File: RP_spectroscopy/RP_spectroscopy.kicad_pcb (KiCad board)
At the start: 2 copper layers, 90.5 x 116.6 mm, 79 parts, among them J1 Extension connector 1, J10 Conn_Coaxial, J2 Extension connector 2, J3 Conn_Coaxial, J4 Conn_Coaxial, J5 Conn_Coaxial, J6 Conn_Coaxial, J7 Molex PicoBlade, J8 Molex PicoBlade, J9 Conn_Coaxial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

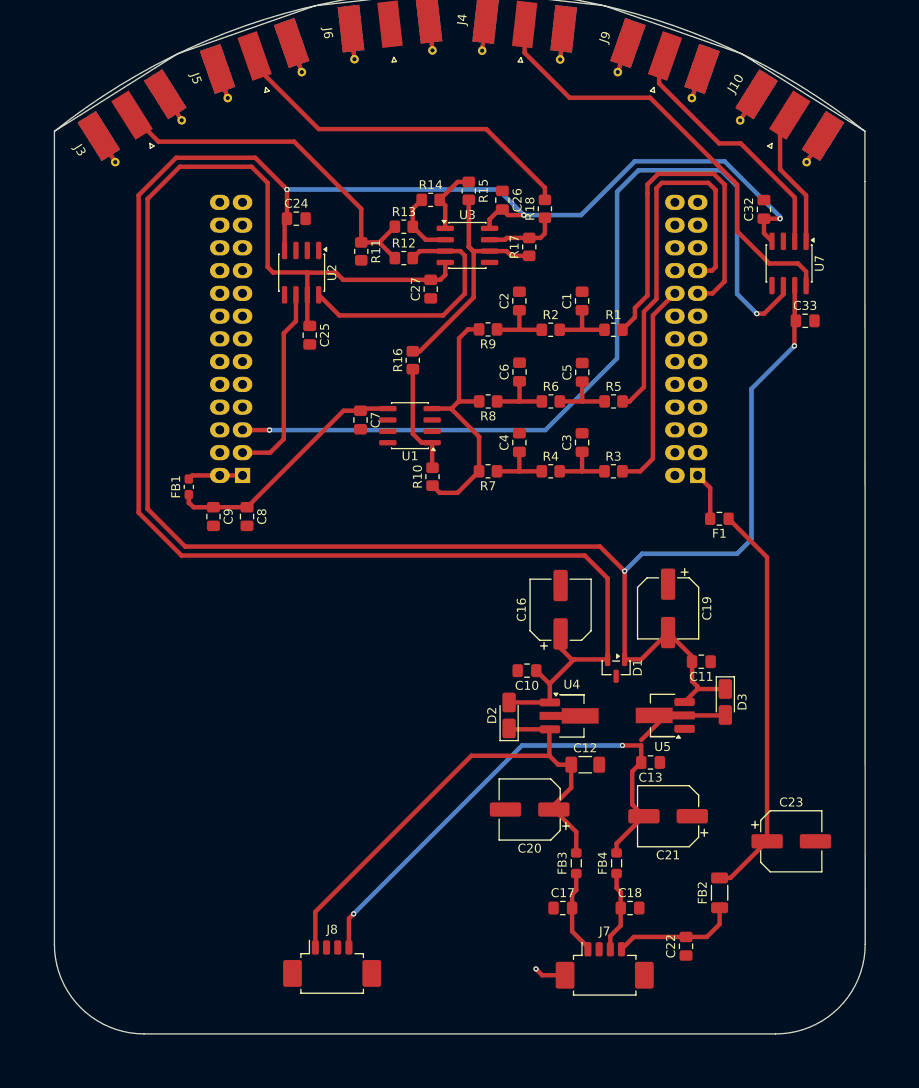
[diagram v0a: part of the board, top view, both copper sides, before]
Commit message: Modified the layout in order to give space in the upper part for the filter + amplification
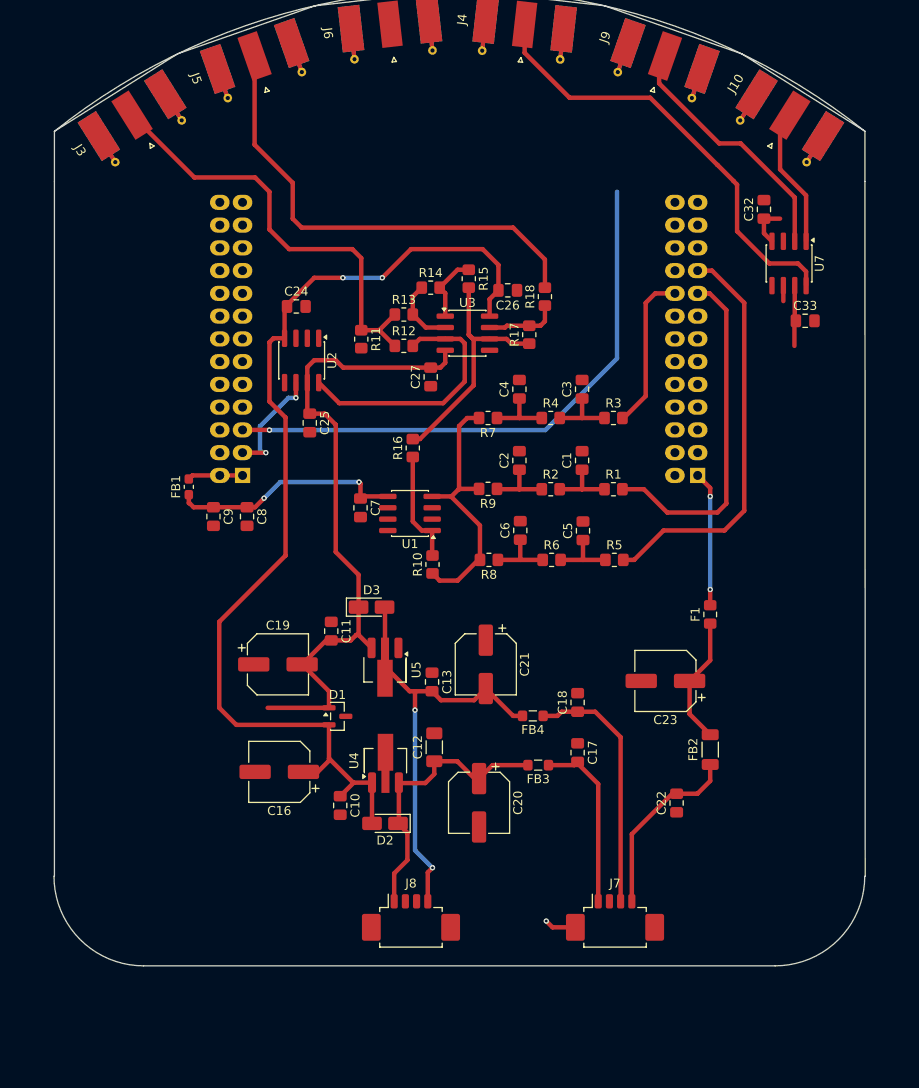
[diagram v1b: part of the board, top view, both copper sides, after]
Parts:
- moved C19 44.0 mm to (115.0, 108.8), turned to 0 degrees
- moved C11 41.5 mm to (120.9, 105.0), turned to -90 degrees
- moved D3 40.9 mm to (125.4, 102.4), turned to 0 degrees
- moved C16 36.2 mm to (115.1, 120.8), turned to 180 degrees
- moved D1 31.6 mm to (121.6, 114.5), turned to 0 degrees
- moved U5 31.4 mm to (126.9, 109.4), turned to -90 degrees
- moved C21 26.5 mm to (138.2, 108.8), turned to -90 degrees
- moved C13 26.0 mm to (132.2, 110.7), turned to -90 degrees
- moved C10 25.7 mm to (121.9, 124.5), turned to -90 degrees
- moved C18 23.7 mm to (148.4, 113.0), turned to 90 degrees
- moved C23 22.8 mm to (158.2, 110.6), turned to 180 degrees
- moved U4 21.4 mm to (127.0, 119.5), turned to 90 degrees
- moved FB4 18.9 mm to (143.4, 114.5), turned to 180 degrees
- moved D2 18.4 mm to (126.9, 126.5), turned to 180 degrees
- moved C1 17.8 mm to (148.9, 86.0)
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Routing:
- net -5VA: track 218.6 -> 80.6 mm, vias 2 -> 0
- net +5VA: track 218.2 -> 121.1 mm, vias 3 -> 2
- net Multiplex switch: track 98.8 -> 64.5 mm, vias 2 -> 1
- net +5V: track 44.8 -> 14.3 mm
- net +15V: track 59.4 -> 32.0 mm
- net Net-(J7-Pin_3): track 9.12 -> 28.3 mm
- net -15V: track 68.6 -> 49.8 mm
- net Summed signals: track 40.4 -> 54.1 mm
- net Net-(J7-Pin_1): track 9.37 -> 19.9 mm
- net Net-(J2-Pin_1): track 5.42 -> 15.1 mm, vias 0 -> 2
- net Sweep/Fast PID: track 40.6 -> 49.7 mm
- net Ramp sign: track 21.9 -> 13.1 mm, vias 0 -> 2
- net Net-(J7-Pin_4): track 13.9 -> 20.5 mm
- net Big offset: track 23.5 -> 17.7 mm
- net Slow integrator: track 41.3 -> 38.7 mm
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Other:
- board size 90.5 x 116.6 mm -> 90.6 x 109 mm

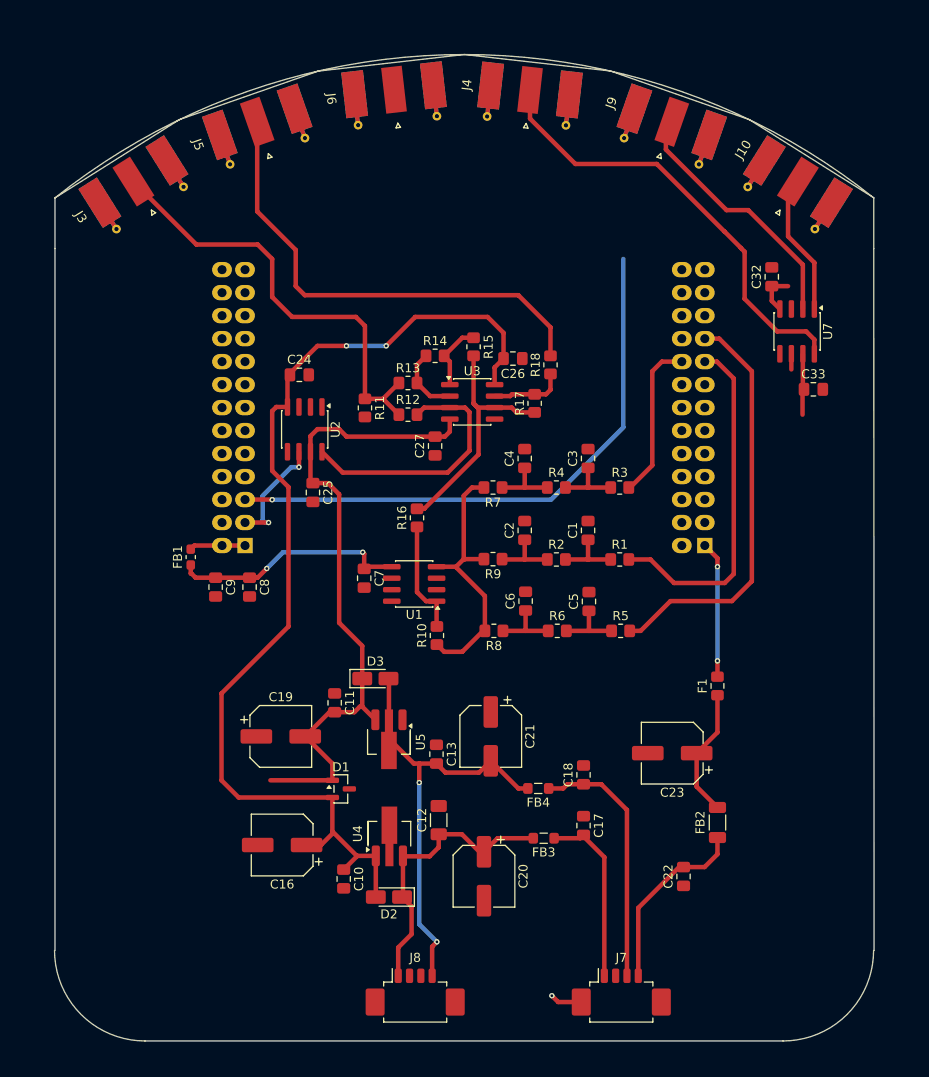
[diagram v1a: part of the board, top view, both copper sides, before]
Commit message: Compacted power and sumator branches. Started to check the RP measurement and compatibility
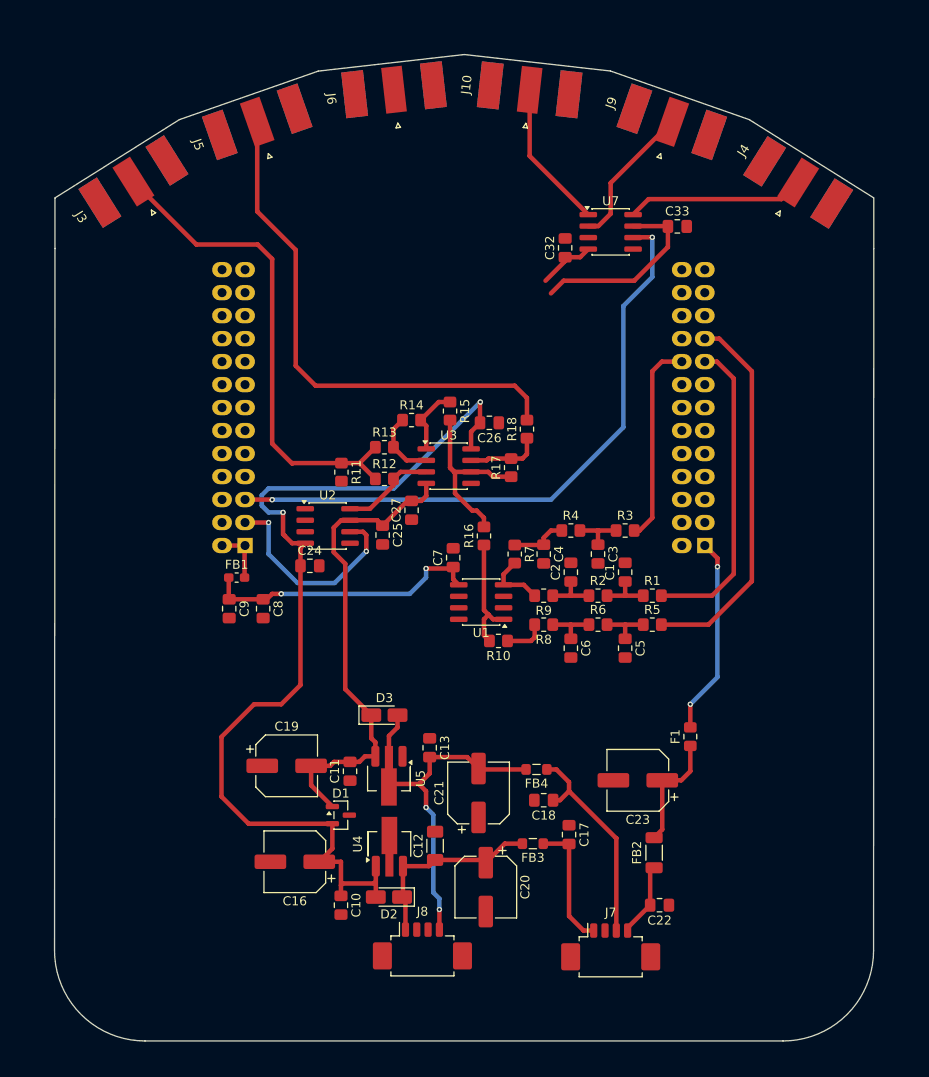
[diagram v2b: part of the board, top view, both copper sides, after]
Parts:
- moved J4 30.6 mm to (171.2, 49.0), turned to -122.169 degrees
- moved J10 30.6 mm to (142.3, 39.0), turned to -96.434 degrees
- moved C33 23.5 mm to (158.8, 52.4)
- moved U7 23.4 mm to (151.4, 53.0), turned to 0 degrees
- moved C32 23.1 mm to (146.4, 54.8)
- moved C24 21.1 mm to (118.2, 89.9)
- moved U2 11.0 mm to (120.1, 85.5), turned to 0 degrees
- moved C4 10.8 mm to (144.0, 88.6), turned to -90 degrees
- moved C3 10.6 mm to (150.0, 88.6), turned to -90 degrees
- moved C7 10.1 mm to (134.0, 89.0), turned to 90 degrees
- moved C25 9.02 mm to (126.2, 86.5)
- moved FB2 7.75 mm to (156.2, 121.6)
- moved C11 7.75 mm to (122.6, 112.6), turned to 90 degrees
- moved R7 7.73 mm to (140.8, 88.6), turned to -90 degrees
- moved R16 7.67 mm to (137.4, 86.6)
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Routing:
- net Differential PD: track 49.3 -> 19.7 mm
- net Net-(U1--): track 30.2 -> 11.4 mm
- net Net-(U3A-+): track 28.8 -> 10.5 mm
- net +/- PD: track 28.6 -> 16.0 mm
- net Net-(J7-Pin_4): track 20.5 -> 8.15 mm
- net +15V: track 32.0 -> 21.7 mm
- net Ramp sign: track 13.1 -> 23.4 mm
- net -15V: track 49.8 -> 42.6 mm
- net Net-(J2-Pin_1): track 15.1 -> 21.9 mm
- net Net-(U3B--): track 27.6 -> 20.8 mm
- net +5VA: track 121.1 -> 115.0 mm
- net Net-(J7-Pin_1): track 19.9 -> 14.2 mm
- net -5VA: track 80.6 -> 75.0 mm
- net Sweep/Fast PID: track 49.7 -> 54.8 mm
- net Multiplex switch: track 64.5 -> 69.6 mm, vias 1 -> 2
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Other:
- board size 90.6 x 109 mm -> 90.5 x 109 mm

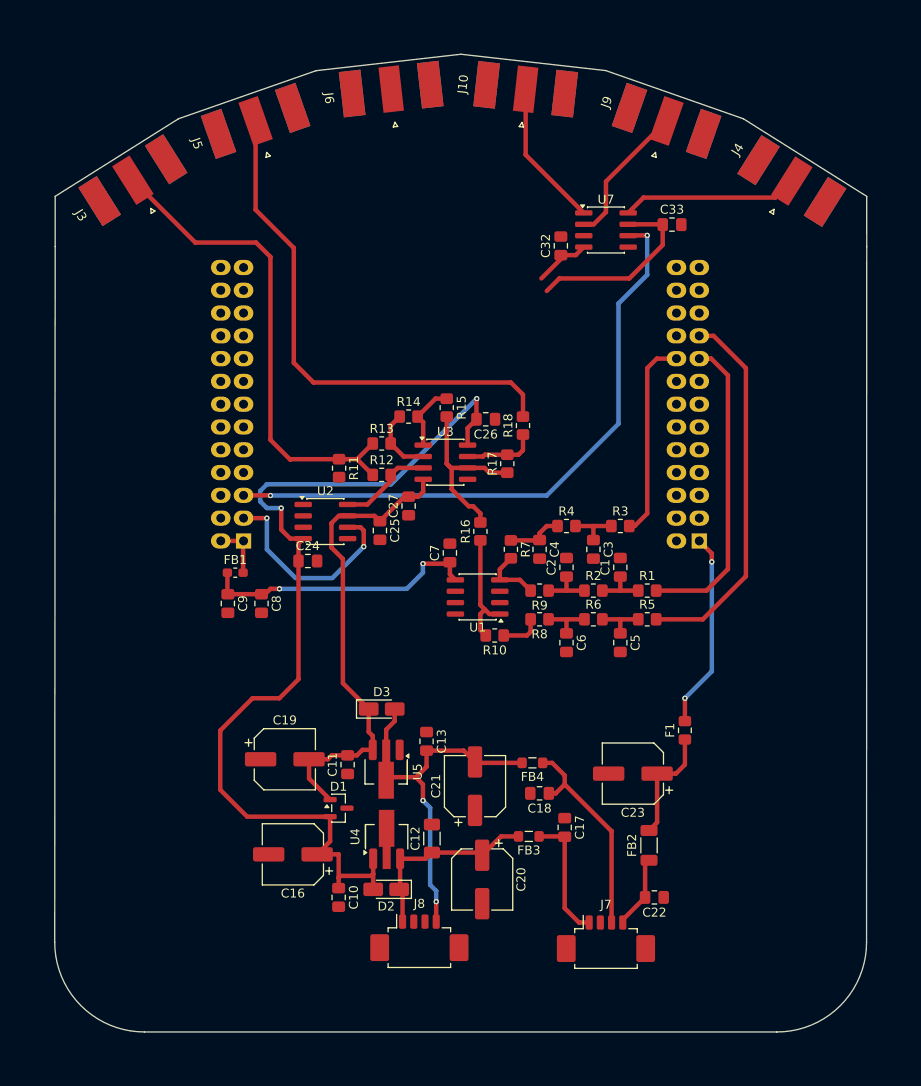
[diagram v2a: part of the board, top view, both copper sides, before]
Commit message: Added the holes aligned with the ones of the RedPitaya. Modified the demultiplex circuit. Optimized the summator wireings.
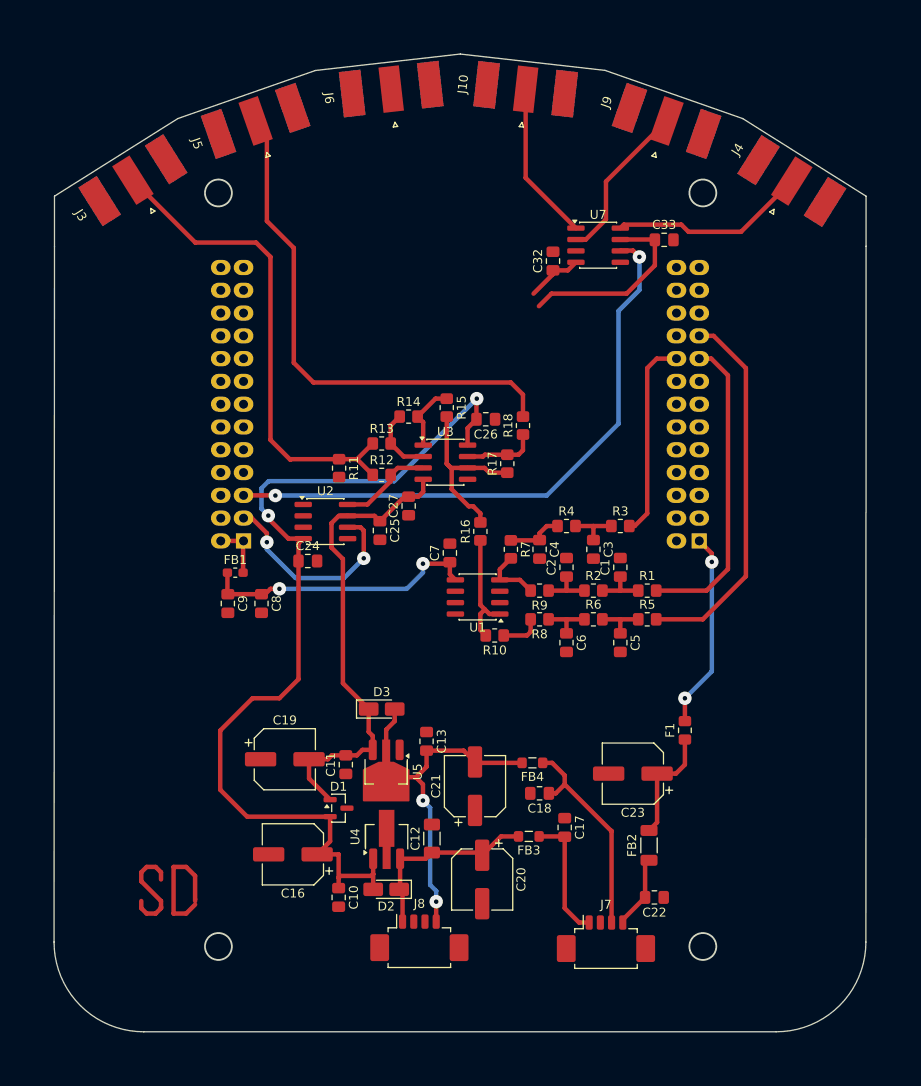
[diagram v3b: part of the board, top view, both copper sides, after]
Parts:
- moved C32 1.91 mm to (145.5, 56.5)
- moved C33 1.91 mm to (157.9, 54.1)
- moved U7 1.91 mm to (150.5, 54.7)
- moved C11 0.20 mm to (122.4, 112.6)
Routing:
- net (no net): track 0.00 -> 25.7 mm
- net Multiplex switch: track 69.6 -> 67.1 mm
- net Differential PD: track 19.7 -> 22.0 mm
- net +/- PD: track 16.0 -> 18.1 mm
- net DC PD demultiplexed signal: track 16.5 -> 17.8 mm
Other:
- outline, holes or cut-outs redrawn
